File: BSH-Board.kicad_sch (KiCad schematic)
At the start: 58 parts, among them J1 667101210103, J2 MICRO QTZB5.0, SW1 TS-3025-B-C-B, SW2 TS-3025-B-C-B, U1 ESP32-C6-MINI-1-N4, U2 AP63203WU, U3 NCP715SQ50T2G, U4 LSF0102DQER

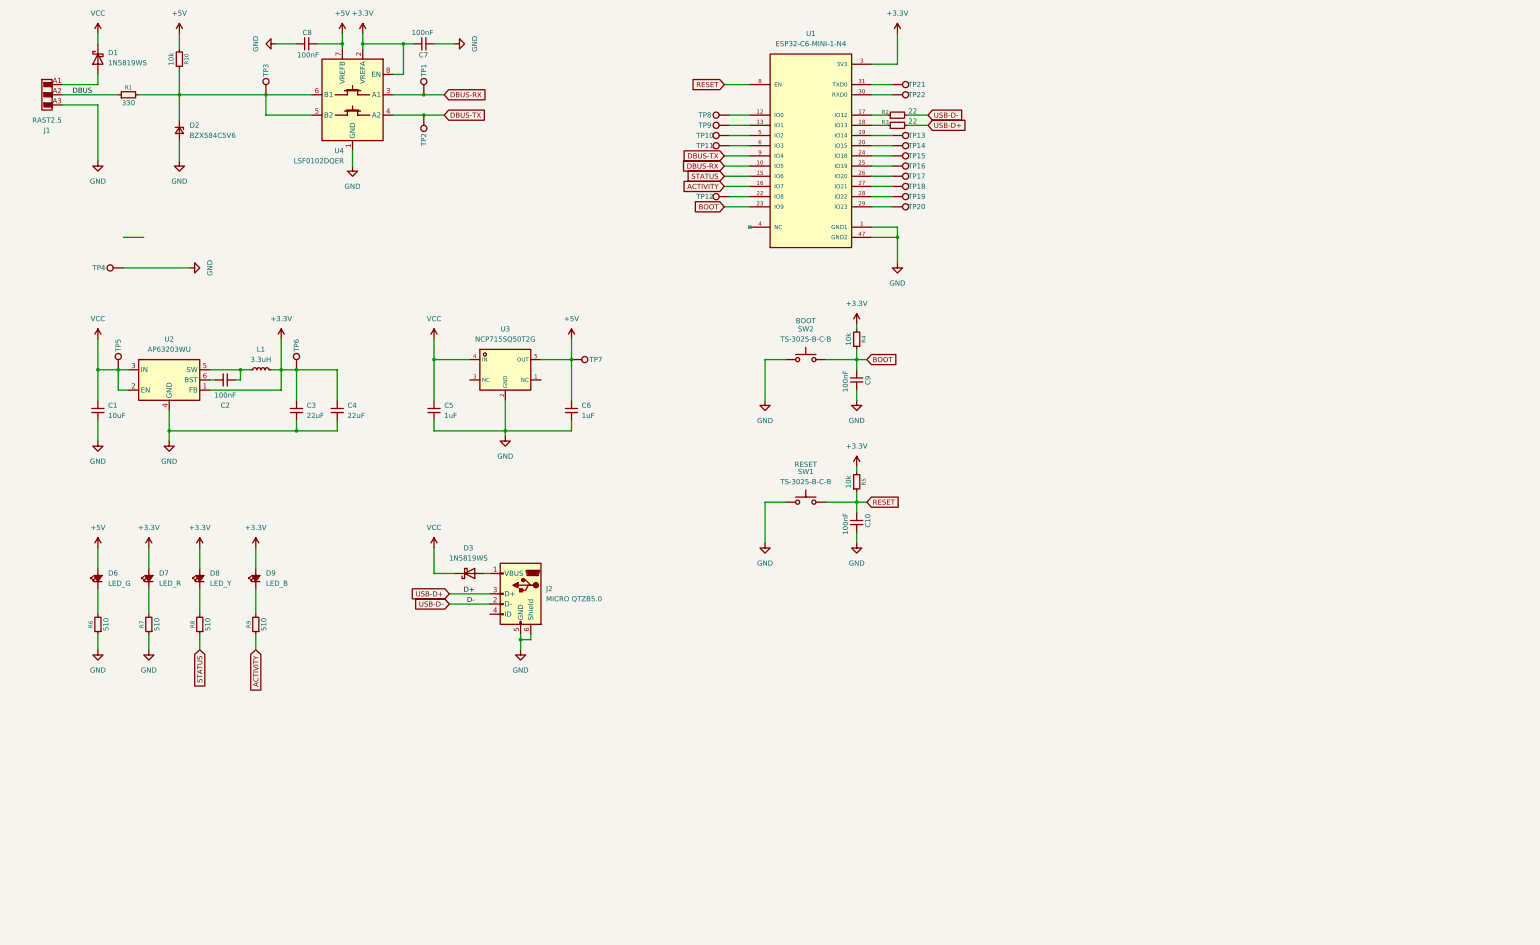
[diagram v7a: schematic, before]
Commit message: Using 74LVC Logic, get rid of LDO for 5V
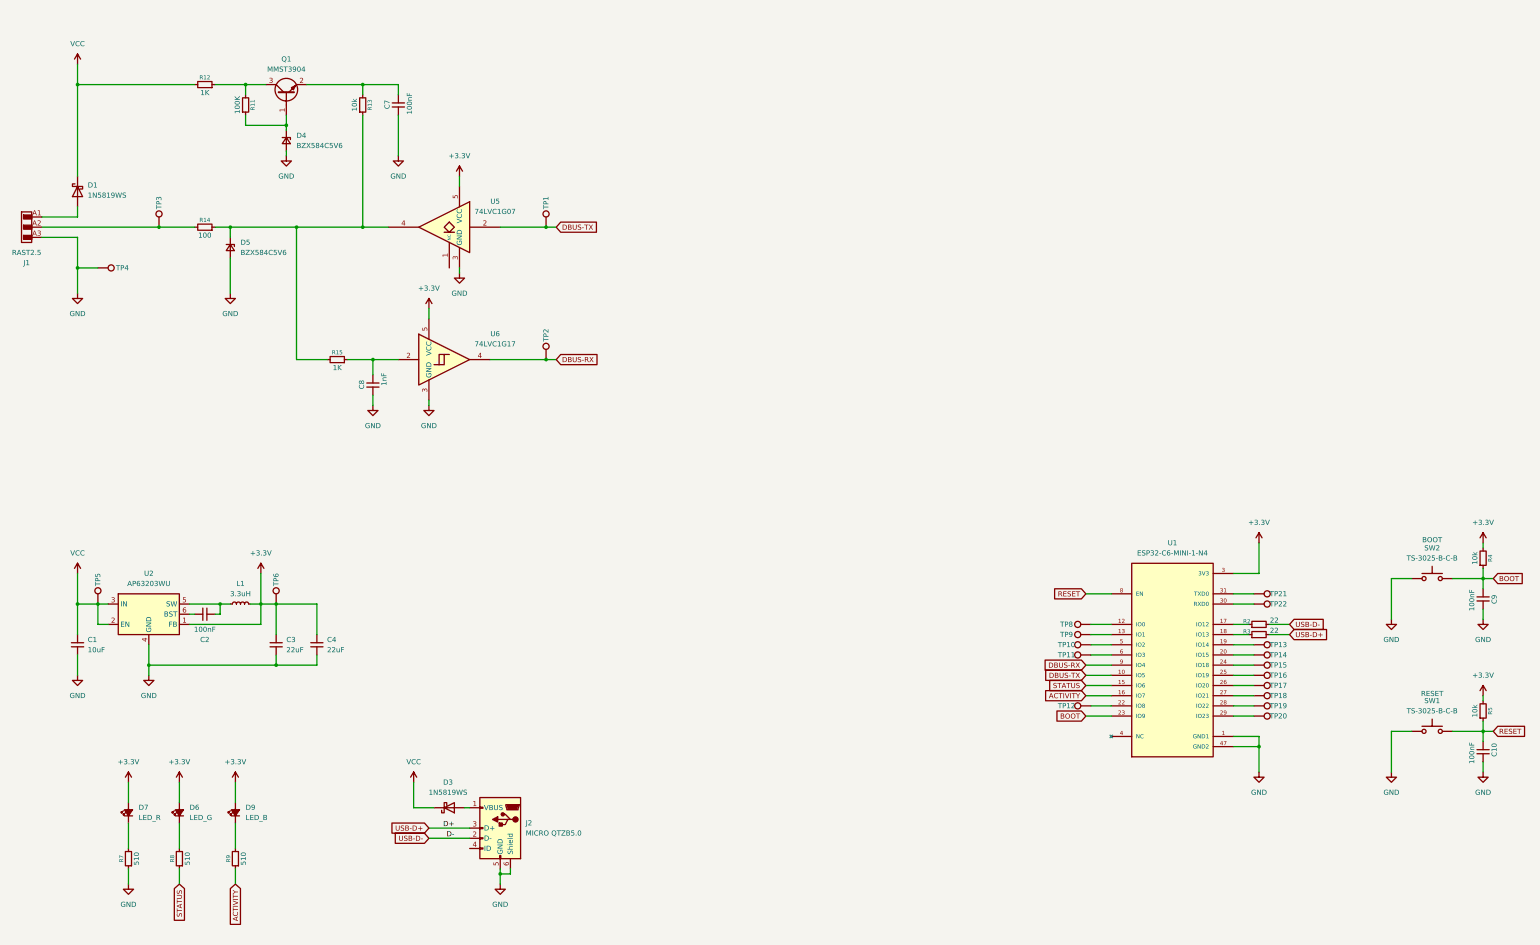
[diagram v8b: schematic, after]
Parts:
- removed C5, C6: 1uF, Capacitor_SMD:C_0402_1005Metric, symbol Device:C_Small
- removed D2: BZX584C5V6, Diode_SMD:D_SOD-523, symbol Device:D_Zener_Small
- removed D8: LED_Y, LED_SMD:LED_0402_1005Metric, symbol Device:LED_Small_Filled
- removed R1: 330, Resistor_SMD:R_0402_1005Metric, symbol Device:R_Small
- removed R10: 10k, Resistor_SMD:R_0402_1005Metric, symbol Device:R_Small
- removed R6: 510, Resistor_SMD:R_0402_1005Metric, symbol Device:R_Small
- removed TP7: TestPoint, Testpoints:TestPoint_Pad_D1.0mm, symbol Connector:TestPoint
- removed U3: NCP715SQ50T2G, Package_TO_SOT_SMD:SOT-353_SC-70-5, symbol NCP715SQ50T2G:NCP715SQ50T2G
- removed U4: LSF0102DQER, Package_SON:X2SON-8_1.4x1mm_P0.35mm, symbol LSF0102DQER:LSF0102DQER
- added D4, D5: BZX584C5V6, Diode_SMD:D_SOD-523, symbol Device:D_Zener_Small
- added Q1: MMST3904, Package_TO_SOT_SMD:SOT-323_SC-70, symbol Transistor_BJT:Q_NPN_BEC
- added R11: 100K, Resistor_SMD:R_0402_1005Metric, symbol Device:R_Small
- added R12, R15: 1K, Resistor_SMD:R_0402_1005Metric, symbol Device:R_Small
- added R13: 10k, Resistor_SMD:R_0402_1005Metric, symbol Device:R_Small
- added R14: 100, Resistor_SMD:R_0402_1005Metric, symbol Device:R_Small
- added U5: 74LVC1G07, Package_TO_SOT_SMD:SOT-353_SC-70-5, symbol 74xGxx:74LVC1G07
- added U6: 74LVC1G17, Package_TO_SOT_SMD:SOT-353_SC-70-5, symbol 74xGxx:74LVC1G17
- C8: value 100nF -> 1nF; LCSC C307331 -> C1523
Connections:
- net DBUS is gone; now on an unnamed net: J1.A2, J1.B2
- net +3.3V: now also D6.2 (A), U5.5 (VCC), U6.5 (VCC); no longer C7.2
- net DBUS-RX: now also TP2.1, U1.9 (IO4), U6.4; no longer TP1.1, U1.10 (IO5)
- net DBUS-TX: now also TP1.1, U1.10 (IO5), U5.2; no longer TP2.1, U1.9 (IO4)
- net GND: now also D4.2 (A), D5.2 (A), U5.3 (GND), U6.3 (GND)
- net VCC: now also R12.2
- net at TP3.1: now also R14.2
- net at D6.1 (K): now also R8.2
- net +5V: no longer names the net of C8.2
- net +5V: now also R15.1, U6.2; no longer D6.2 (A)
- new net: D5.1 (K), R13.1, R14.1, R15.2, U5.4
- new net: D4.1 (K), Q1.1 (B), R11.1
- new net: Q1.3 (C), R11.2, R12.1
- new net: C7.2, Q1.2 (E), R13.2
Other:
- moved on the sheet: C1, C10, C2, C3, C4, C7, C8, C9, D1, D3, D6, D7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
